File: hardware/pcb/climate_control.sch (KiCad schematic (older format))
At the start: 43 parts, among them J1 Switch, J2 BatteryIn, J3 USB_C, J4 HeatElement, J5 ICSP, Q1 NTR3C21NZ, Q2 NTR3C21NZ, U1 TP4056, U2 XB8089A, U3 ATmega328PB-AU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

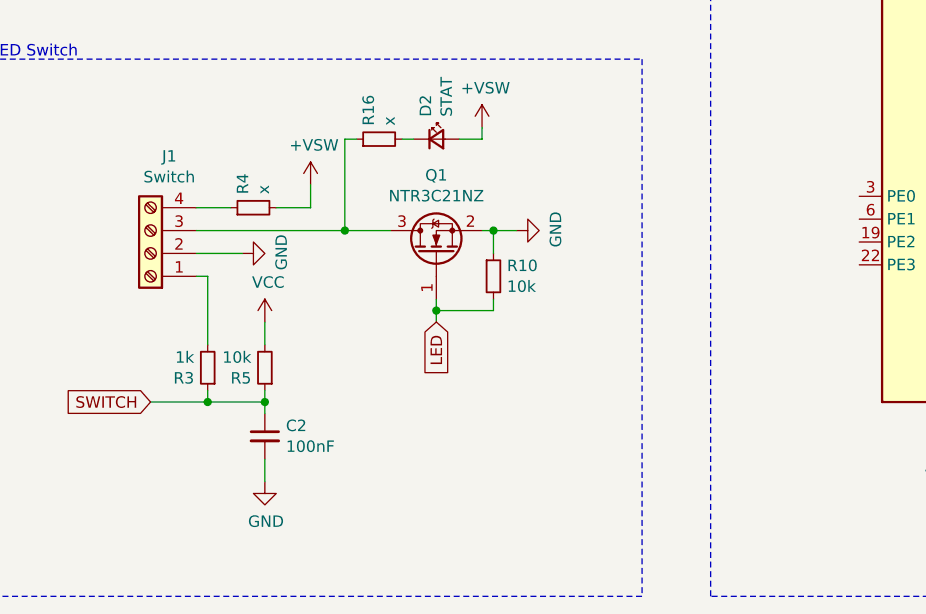
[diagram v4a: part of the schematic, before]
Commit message: Added comments on LED/Switch circuitry
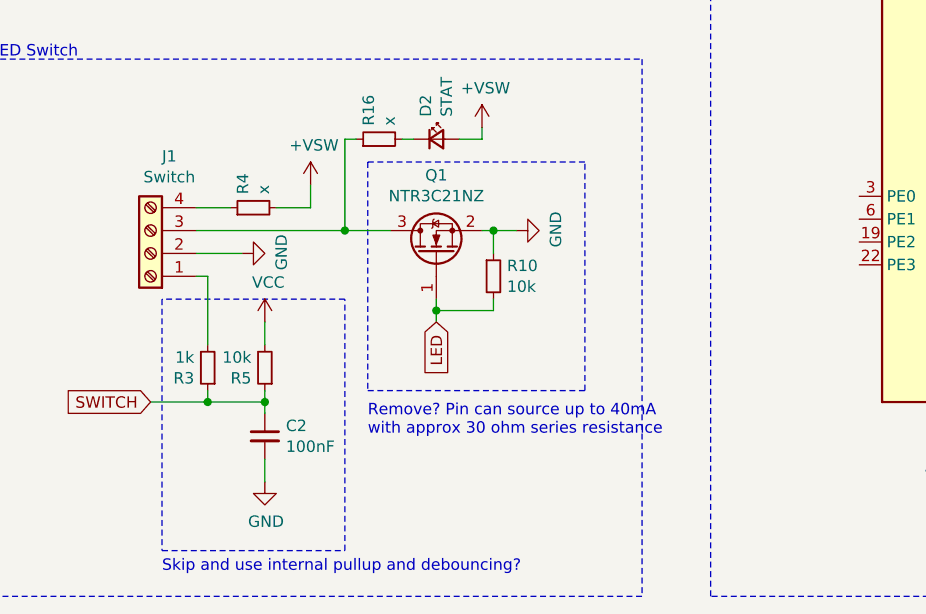
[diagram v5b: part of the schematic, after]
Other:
- note added: "Remove? Pin can source up to 40mA\nwith approx 30 ohm series resistance"
- note added: "Skip and use internal pullup and debouncing?"
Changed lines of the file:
@@
 Wire Wire Line
 	1950 3000 1950 3300
+Wire Notes Line
+	2250 10100 2250 9000
+Wire Notes Line
+	2250 9000 1450 9000
+Wire Notes Line
+	1450 9000 1450 10100
+Wire Notes Line
+	1450 10100 2250 10100
+Text Notes 1450 10200 0    50   ~ 0
+Skip and use internal pullup and debouncing?
+Wire Notes Line
+	3300 9400 3300 8400
+Wire Notes Line
+	3300 8400 2350 8400
+Wire Notes Line
+	2350 8400 2350 9400
+Wire Notes Line
+	2350 9400 3300 9400
+Text Notes 2350 9600 0    50   ~ 0
+Remove? Pin can source up to 40mA\nwith approx 30 ohm series resistance
 $EndSCHEMATC

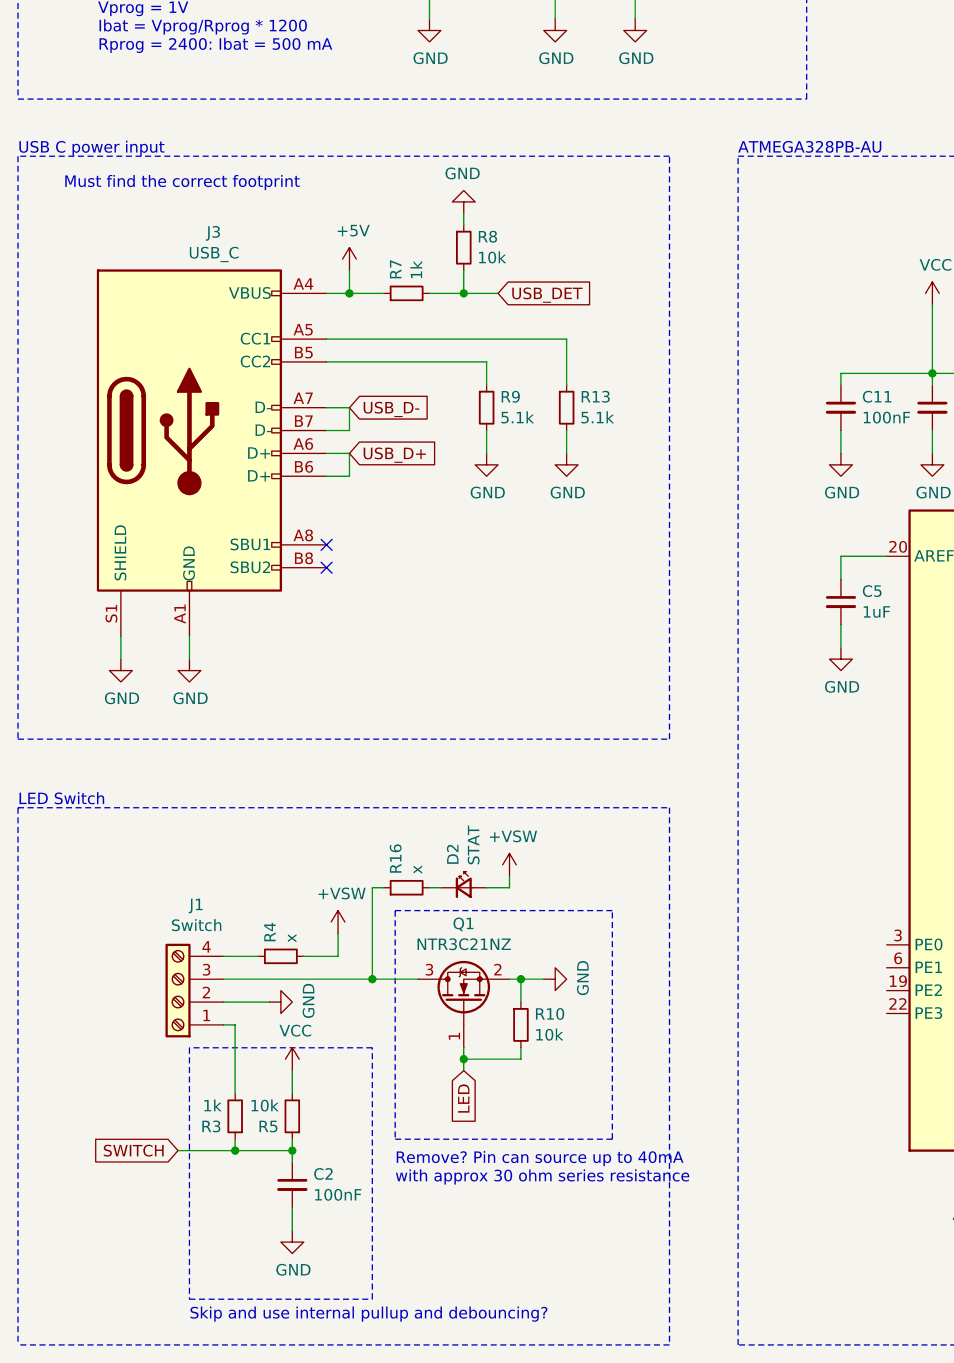
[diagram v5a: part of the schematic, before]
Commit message: Removed unnececary components
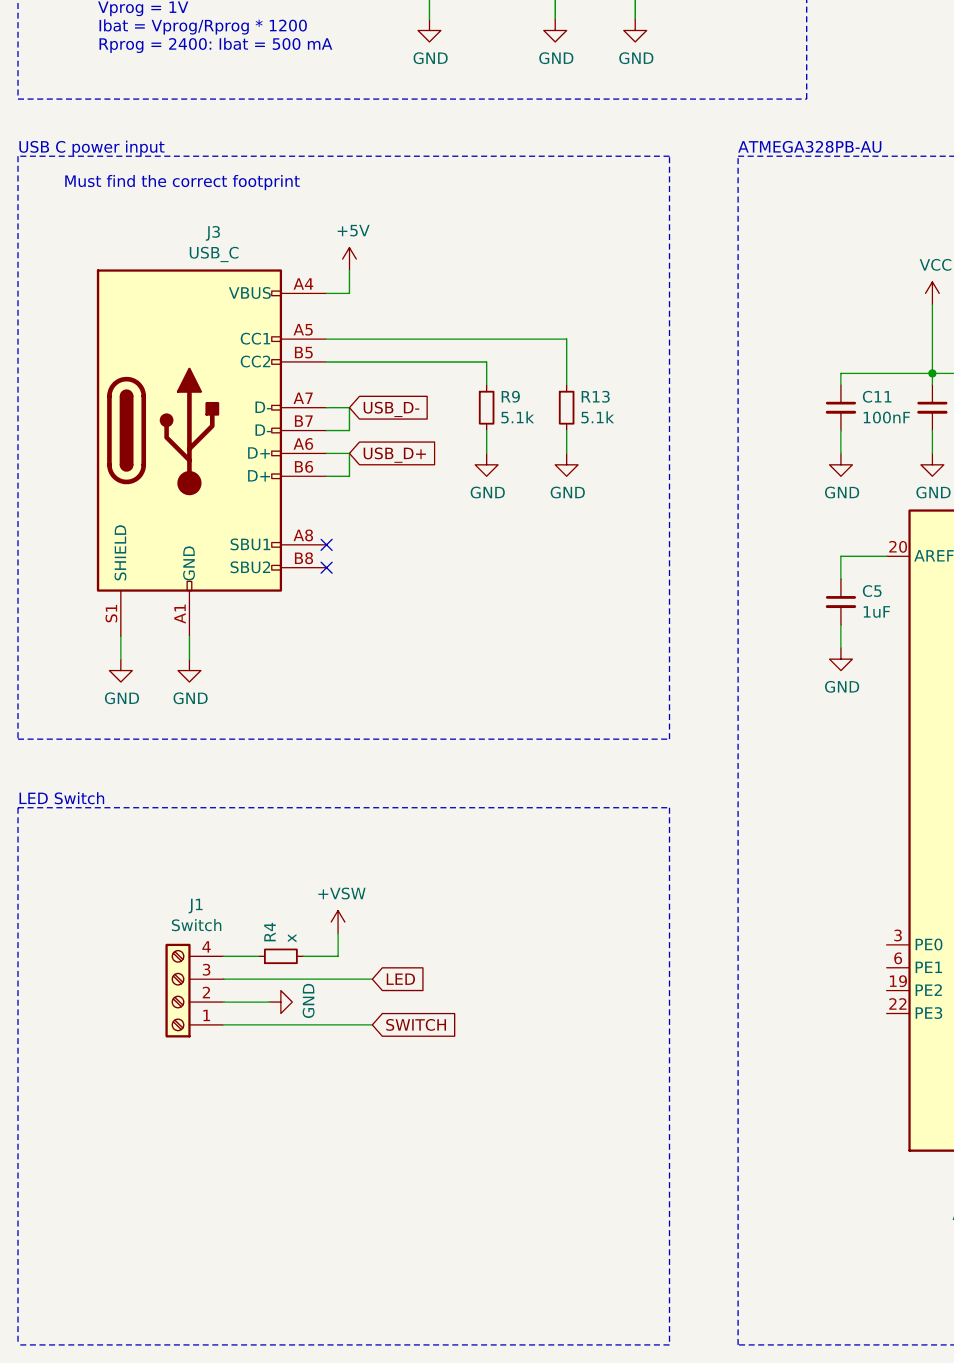
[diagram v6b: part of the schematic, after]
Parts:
- removed C2: 100nF, Capacitor_SMD:C_0402_1005Metric, symbol Device:C_Small
- removed D2: STAT, Diode_SMD:D_0603_1608Metric, symbol Device:LED_Small
- removed Q1: NTR3C21NZ, Package_TO_SOT_SMD:SOT-23, symbol Device:Q_NMOS_GSD
- removed R10, R5, R8: 10k, Resistor_SMD:R_0402_1005Metric, symbol Device:R_Small
- removed R16: x, Resistor_SMD:R_0402_1005Metric, symbol Device:R_Small
- removed R3, R7: 1k, Resistor_SMD:R_0402_1005Metric, symbol Device:R_Small
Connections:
- net LED: now also J1.3 (Pin_3)
- net SWITCH: now also J1.1 (Pin_1)
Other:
- note removed: "Remove? Pin can source up to 40mA\nwith approx 30 ohm series resistance"
- note removed: "Skip and use internal pullup and debouncing?"

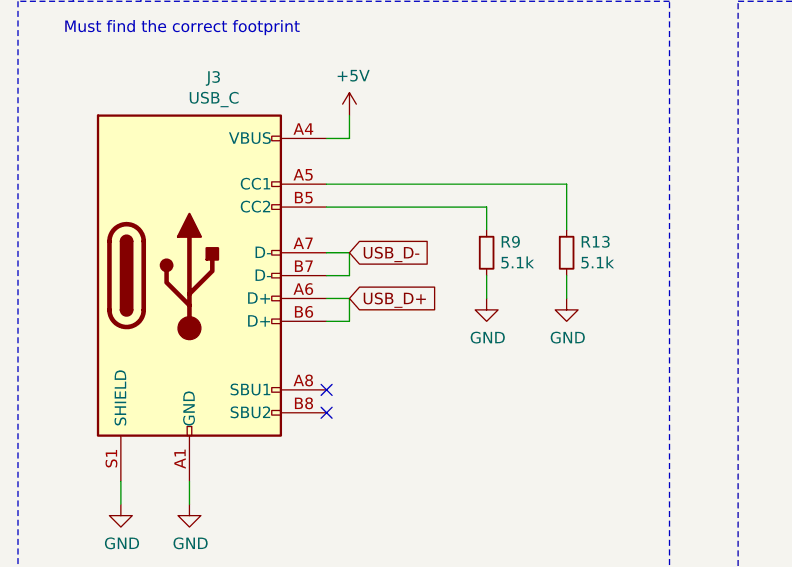
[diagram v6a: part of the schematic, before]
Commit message: Routing complete and added some silkscreen.
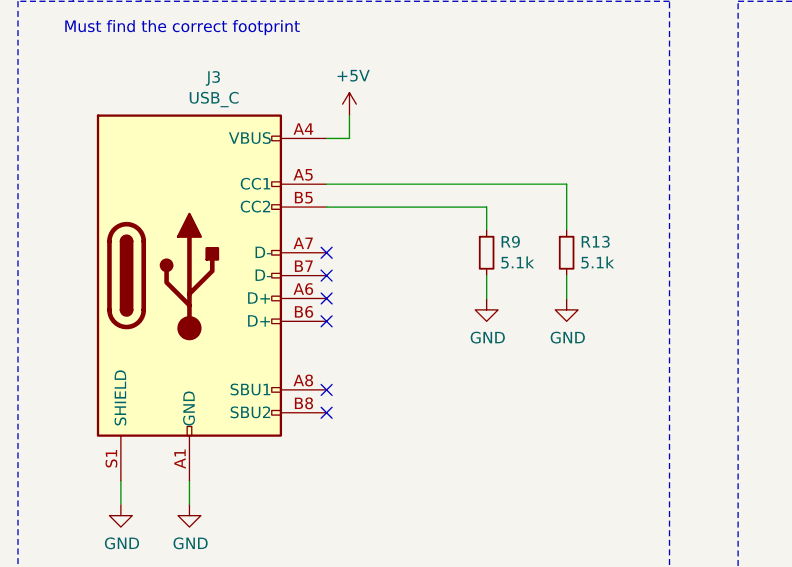
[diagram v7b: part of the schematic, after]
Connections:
- net USB_D+: no longer names the net of J3.A6 (D+)
- net USB_D+: no longer J3.B6 (D+)
- net USB_D-: no longer names the net of J3.A7 (D-)
- net USB_D-: no longer J3.B7 (D-)
- no-connect marks 5 -> 9
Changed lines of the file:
@@
 Wire Wire Line
 	3100 6400 3100 6300
-Wire Wire Line
-	2050 6200 2150 6200
-Wire Wire Line
-	2150 6200 2150 6300
-Wire Wire Line
-	2150 6300 2050 6300
-Wire Wire Line
-	2050 6400 2150 6400
-Wire Wire Line
-	2150 6400 2150 6500
-Wire Wire Line
-	2150 6500 2050 6500
-Text GLabel 2150 6200 2    50   Input ~ 0
-USB_D-
-Text GLabel 2150 6400 2    50   Input ~ 0
-USB_D+
 NoConn ~ 2050 6800
 NoConn ~ 2050 6900
@@
 Wire Wire Line
 	1600 8900 2250 8900
+NoConn ~ 2050 6200
+NoConn ~ 2050 6300
+NoConn ~ 2050 6400
+NoConn ~ 2050 6500
 $EndSCHEMATC

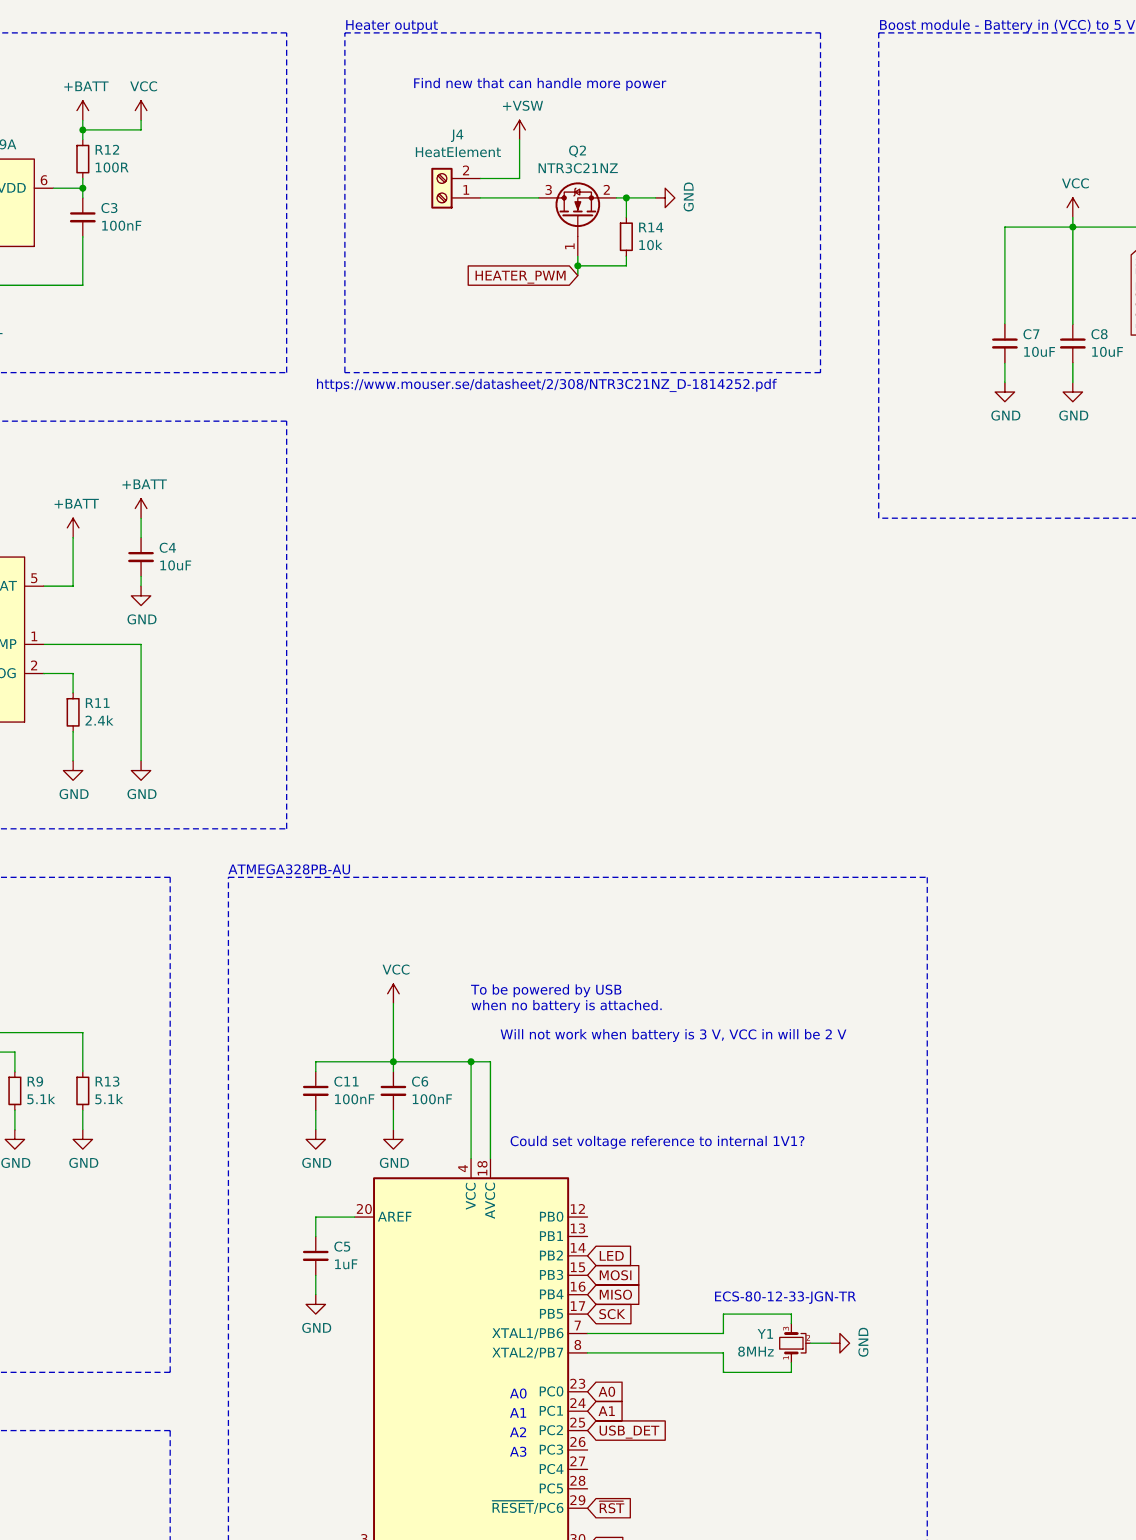
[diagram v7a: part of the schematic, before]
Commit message: Added battery divider to MCU.
A voltage divider from the battery is now connected to the MCU.
The divider is designed to work with the internal voltage reference (1V1).
With the resistor values, a battery voltage of 5 V will be 1.15 at MCU.
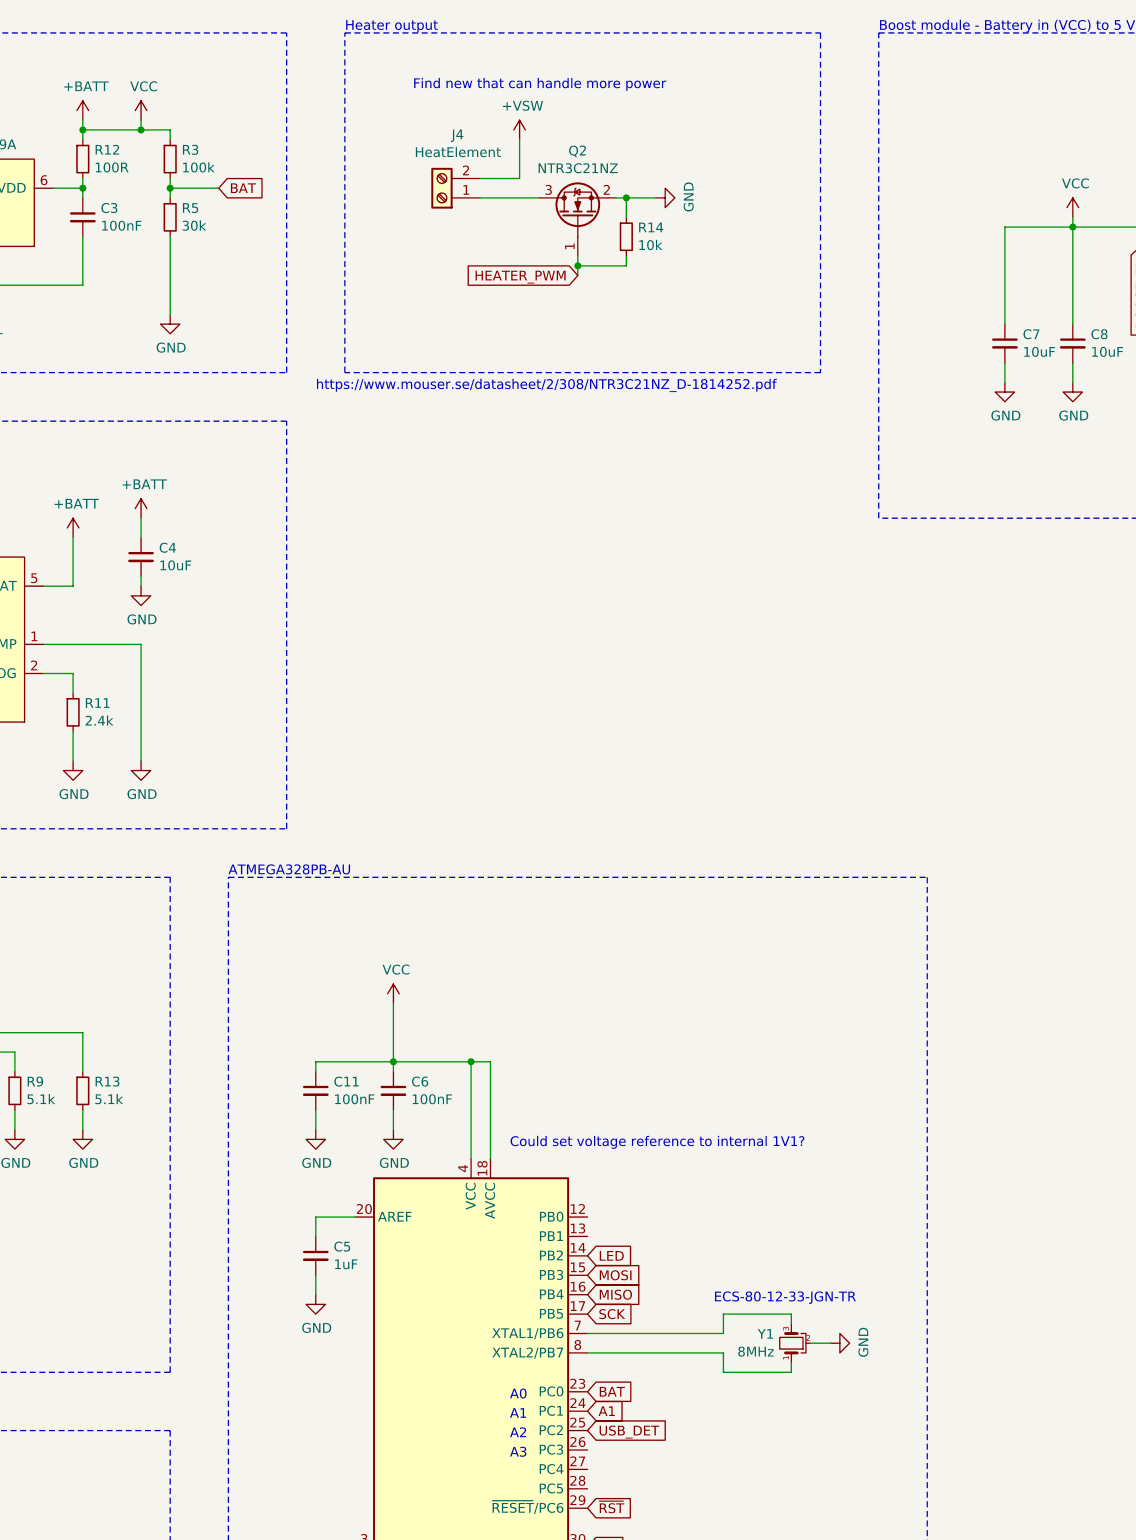
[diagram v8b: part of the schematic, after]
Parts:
- added R3: 100k, Resistor_SMD:R_0402_1005Metric, symbol Device:R_Small
- added R5: 30k, Resistor_SMD:R_0402_1005Metric, symbol Device:R_Small
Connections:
- net +BATT: now also R3.1
- net GND: now also R5.2
- net A0 renamed BAT
- net BAT: now also R3.2, R5.1
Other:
- note removed: "To be powered by USB \nwhen no battery is attached."
- note removed: "Will not work when battery is 3 V, VCC in will be 2 V"
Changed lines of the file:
@@
 Text GLabel 2250 8900 2    50   Input ~ 0
 SWITCH
-Text Notes 5100 5800 0    50   ~ 0
-To be powered by USB \nwhen no battery is attached.
 $Comp
 L power:+VSW #PWR0140
@@
 Text Notes 3850 5100 0    50   ~ 0
 ATMEGA328PB-AU
-Text GLabel 5700 7750 2    50   Input ~ 0
-A0
 Text GLabel 5700 7850 2    50   Input ~ 0
 A1
@@
 Text Notes 1650 3900 0    50   ~ 0
 5mA
-Text Notes 5250 5950 0    50   ~ 0
-Will not work when battery is 3 V, VCC in will be 2 V
 Wire Wire Line
 	4700 5750 4700 6050
@@
 NoConn ~ 2050 6400
 NoConn ~ 2050 6500
+Text GLabel 5700 7750 2    50   Input ~ 0
+BAT
+$Comp
+L Device:R_Small R3
+U 1 1 6036D9D3
+P 3550 1400
+F 0 "R3" H 3609 1446 50  0000 L CNN
+F 1 "100k" H 3609 1355 50  0000 L CNN
+F 2 "Resistor_SMD:R_0402_1005Metric" H 3550 1400 50  0001 C CNN
+F 3 "~" H 3550 1400 50  0001 C CNN
+	1    3550 1400
+	1    0    0    -1
+$EndComp
+$Comp
+L Device:R_Small R5
+U 1 1 6036DDB8
+P 3550 1700
+F 0 "R5" H 3609 1746 50  0000 L CNN
+F 1 "30k" H 3609 1655 50  0000 L CNN
+F 2 "Resistor_SMD:R_0402_1005Metric" H 3550 1700 50  0001 C CNN
+F 3 "~" H 3550 1700 50  0001 C CNN
+	1    3550 1700
+	1    0    0    -1
+$EndComp
+$Comp
+L power:GND #PWR0134
+U 1 1 6036E180
+P 3550 2200
+F 0 "#PWR0134" H 3550 1950 50  0001 C CNN
+F 1 "GND" H 3555 2027 50  0000 C CNN
+F 2 "" H 3550 2200 50  0001 C CNN
+F 3 "" H 3550 2200 50  0001 C CNN
+	1    3550 2200
+	1    0    0    -1
+$EndComp
+Wire Wire Line
+	3550 1600 3550 1550
+Wire Wire Line
+	3550 1300 3550 1250
+Wire Wire Line
+	3550 1250 3400 1250
+Connection ~ 3400 1250
+Text GLabel 3800 1550 2    50   Input ~ 0
+BAT
+Connection ~ 3550 1550
+Wire Wire Line
+	3550 1550 3550 1500
+Wire Wire Line
+	3550 1800 3550 2200
+Wire Wire Line
+	3550 1550 3800 1550
 $EndSCHEMATC
